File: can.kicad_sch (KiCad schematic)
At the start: 0 parts

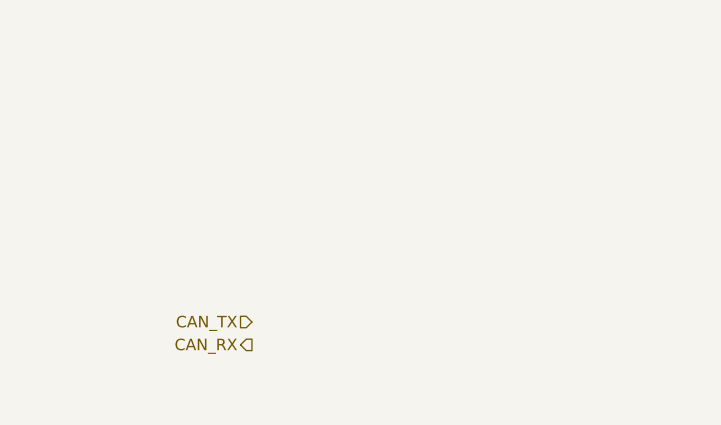
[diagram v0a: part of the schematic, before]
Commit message: Finish schematic
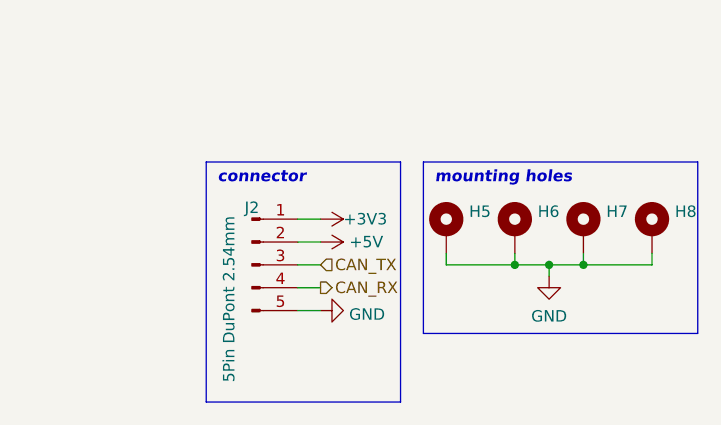
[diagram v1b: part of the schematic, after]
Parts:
- added H5, H6, H7, H8: MountingHole_Pad, MountingHole:MountingHole_3.2mm_M3_Pad_Via, symbol Mechanical:MountingHole_Pad
- added J2: 5Pin DuPont 2.54mm, Connector_PinHeader_2.54mm:PinHeader_1x05_P2.54mm_Vertical, symbol Connector:Conn_01x05_Male
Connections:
- net CAN_RX: now also J2.4 (Pin_4)
- net CAN_TX: now also J2.3 (Pin_3)
- new net +3V3: J2.1 (Pin_1)
- new net +5V: J2.2 (Pin_2)
- new net GND: H5.1, H6.1, H7.1, H8.1, J2.5 (Pin_5)
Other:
- note added: "connector"
- note added: "mounting holes"
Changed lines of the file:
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@@
 (kicad_sch (version 20211123) (generator eeschema)
   (paper "A4")
+  (junction (at 144.78 71.12) (diameter 0) (color 0 0 0 0)
+  )
+  (junction (at 140.97 71.12) (diameter 0) (color 0 0 0 0)
+  )
+  (junction (at 137.16 71.12) (diameter 0) (color 0 0 0 0)
+  )
+  (wire (pts (xy 144.78 71.12) (xy 152.4 71.12))
+    (stroke (width 0) (type default) (color 0 0 0 0))
+  )
+  (wire (pts (xy 113.03 76.2) (xy 115.57 76.2))
+    (stroke (width 0) (type default) (color 0 0 0 0))
+  )
+  (wire (pts (xy 113.03 73.66) (xy 115.57 73.66))
+    (stroke (width 0) (type default) (color 0 0 0 0))
+  )
+  (wire (pts (xy 137.16 69.85) (xy 137.16 71.12))
+    (stroke (width 0) (type default) (color 0 0 0 0))
+  )
+  (polyline (pts (xy 127 59.69) (xy 157.48 59.69))
+    (stroke (width 0) (type default) (color 0 0 0 0))
+  )
+  (polyline (pts (xy 157.48 78.74) (xy 157.48 59.69))
+    (stroke (width 0) (type default) (color 0 0 0 0))
+  )
+  (polyline (pts (xy 102.87 86.36) (xy 124.46 86.36))
+    (stroke (width 0) (type default) (color 0 0 0 0))
+  )
+  (wire (pts (xy 152.4 71.12) (xy 152.4 69.85))
+    (stroke (width 0) (type default) (color 0 0 0 0))
+  )
+  (wire (pts (xy 144.78 69.85) (xy 144.78 71.12))
+    (stroke (width 0) (type default) (color 0 0 0 0))
+  )
+  (wire (pts (xy 113.03 71.12) (xy 115.57 71.12))
+    (stroke (width 0) (type default) (color 0 0 0 0))
+  )
+  (wire (pts (xy 113.03 66.04) (xy 115.57 66.04))
+    (stroke (width 0) (type default) (color 0 0 0 0))
+  )
+  (polyline (pts (xy 102.87 59.69) (xy 124.46 59.69))
+    (stroke (width 0) (type default) (color 0 0 0 0))
+  )
+  (wire (pts (xy 140.97 71.12) (xy 140.97 72.39))
+    (stroke (width 0) (type default) (color 0 0 0 0))
+  )
+  (polyline (pts (xy 124.46 86.36) (xy 124.46 59.69))
+    (stroke (width 0) (type default) (color 0 0 0 0))
+  )
+  (wire (pts (xy 129.54 69.85) (xy 129.54 71.12))
+    (stroke (width 0) (type default) (color 0 0 0 0))
+  )
+  (wire (pts (xy 140.97 71.12) (xy 144.78 71.12))
+    (stroke (width 0) (type default) (color 0 0 0 0))
+  )
+  (wire (pts (xy 113.03 68.58) (xy 115.57 68.58))
+    (stroke (width 0) (type default) (color 0 0 0 0))
+  )
+  (polyline (pts (xy 127 59.69) (xy 127 78.74))
+    (stroke (width 0) (type default) (color 0 0 0 0))
+  )
+  (polyline (pts (xy 127 78.74) (xy 157.48 78.74))
+    (stroke (width 0) (type default) (color 0 0 0 0))
+  )
+  (wire (pts (xy 129.54 71.12) (xy 137.16 71.12))
+    (stroke (width 0) (type default) (color 0 0 0 0))
+  )
+  (polyline (pts (xy 102.87 59.69) (xy 102.87 86.36))
+    (stroke (width 0) (type default) (color 0 0 0 0))
+  )
+  (wire (pts (xy 137.16 71.12) (xy 140.97 71.12))
+    (stroke (width 0) (type default) (color 0 0 0 0))
+  )
+  (text "mounting holes" (at 128.27 62.23 0)
+    (effects (font (size 1.27 1.27) bold italic) (justify left bottom))
+  )
   (text "CAN requierements:\n- galvanic isolation\n- isolated DC/DC converter\n- base is a dedicated PCB due \n  different chip/converter impl. \n  (because semiconductor componts are rare)\n"
     (at 13.97 29.21 0)
     (effects (font (size 1.5 1.5)) (justify left bottom))
   )
-  (hierarchical_label "CAN_TX" (shape input) (at 107.95 77.47 180)
-    (effects (font (size 1.27 1.27)) (justify right))
-  )
-  (hierarchical_label "CAN_RX" (shape output) (at 107.95 80.01 180)
-    (effects (font (size 1.27 1.27)) (justify right))
+  (text "connector" (at 104.14 62.23 0)
+    (effects (font (size 1.27 1.27) bold italic) (justify left bottom))
+  )
+  (hierarchical_label "CAN_TX" (shape input) (at 115.57 71.12 0)
+    (effects (font (size 1.27 1.27)) (justify left))
+  )
+  (hierarchical_label "CAN_RX" (shape output) (at 115.57 73.66 0)
+    (effects (font (size 1.27 1.27)) (justify left))
+  )
+  (symbol (lib_id "Mechanical:MountingHole_Pad") (at 137.16 67.31 0) (unit 1)
+    (in_bom yes) (on_board yes) (fields_autoplaced)
+    (property "Reference" "H6" (id 0) (at 139.7 65.2053 0)
+      (effects (font (size 1.27 1.27)) (justify left))
+    )
+    (property "Value" "MountingHole_Pad" (id 1) (at 139.7 67.7422 0)
+      (effects (font (size 1.27 1.27)) (justify left) hide)
+    )
+    (property "Footprint" "MountingHole:MountingHole_3.2mm_M3_Pad_Via" (id 2) (at 137.16 67.31 0)
+      (effects (font (size 1.27 1.27)) hide)
+    )
+    (property "Datasheet" "~" (id 3) (at 137.16 67.31 0)
+      (effects (font (size 1.27 1.27)) hide)
+    )
+    (pin "1")
+  )
+  (symbol (lib_id "power:+5V") (at 115.57 68.58 270) (unit 1)
+    (in_bom yes) (on_board yes)
+    (property "Reference" "#PWR019" (id 0) (at 111.76 68.58 0)
+      (effects (font (size 1.27 1.27)) hide)
+    )
+    (property "Value" "+5V" (id 1) (at 120.65 68.58 90))
+    (property "Footprint" "" (id 2) (at 115.57 68.58 0)
+      (effects (font (size 1.27 1.27)) hide)
+    )
+    (property "Datasheet" "" (id 3) (at 115.57 68.58 0)
+      (effects (font (size 1.27 1.27)) hide)
+    )
+    (pin "1")
+  )
+  (symbol (lib_id "power:GND") (at 115.57 76.2 90) (unit 1)
+    (in_bom yes) (on_board yes) (fields_autoplaced)
+    (property "Reference" "#PWR021" (id 0) (at 121.92 76.2 0)
+      (effects (font (size 1.27 1.27)) hide)
+    )
+    (property "Value" "GND" (id 1) (at 118.745 76.6338 90)
+      (effects (font (size 1.27 1.27)) (justify right))
+    )
+    (property "Footprint" "" (id 2) (at 115.57 76.2 0)
+      (effects (font (size 1.27 1.27)) hide)
+    )
+    (property "Datasheet" "" (id 3) (at 115.57 76.2 0)
+      (effects (font (size 1.27 1.27)) hide)
+    )
+    (pin "1")
+  )
+  (symbol (lib_id "power:GND") (at 140.97 72.39 0) (unit 1)
+    (in_bom yes) (on_board yes) (fields_autoplaced)
+    (property "Reference" "#PWR020" (id 0) (at 140.97 78.74 0)
+      (effects (font (size 1.27 1.27)) hide)
+    )
+    (property "Value" "GND" (id 1) (at 140.97 76.8334 0))
+    (property "Footprint" "" (id 2) (at 140.97 72.39 0)
+      (effects (font (size 1.27 1.27)) hide)
+    )
+    (property "Datasheet" "" (id 3) (at 140.97 72.39 0)
+      (effects (font (size 1.27 1.27)) hide)
+    )
+    (pin "1")
+  )
+  (symbol (lib_id "Mechanical:MountingHole_Pad") (at 152.4 67.31 0) (unit 1)
+    (in_bom yes) (on_board yes) (fields_autoplaced)
+    (property "Reference" "H8" (id 0) (at 154.94 65.2053 0)
+      (effects (font (size 1.27 1.27)) (justify left))
+    )
+    (property "Value" "MountingHole_Pad" (id 1) (at 154.94 67.7422 0)
+      (effects (font (size 1.27 1.27)) (justify left) hide)
+    )
+    (property "Footprint" "MountingHole:MountingHole_3.2mm_M3_Pad_Via" (id 2) (at 152.4 67.31 0)
+      (effects (font (size 1.27 1.27)) hide)
+    )
+    (property "Datasheet" "~" (id 3) (at 152.4 67.31 0)
+      (effects (font (size 1.27 1.27)) hide)
+    )
+    (pin "1")
+  )
+  (symbol (lib_id "Mechanical:MountingHole_Pad") (at 144.78 67.31 0) (unit 1)
+    (in_bom yes) (on_board yes) (fields_autoplaced)
+    (property "Reference" "H7" (id 0) (at 147.32 65.2053 0)
+      (effects (font (size 1.27 1.27)) (justify left))
+    )
+    (property "Value" "MountingHole_Pad" (id 1) (at 147.32 67.7422 0)
+      (effects (font (size 1.27 1.27)) (justify left) hide)
+    )
+    (property "Footprint" "MountingHole:MountingHole_3.2mm_M3_Pad_Via" (id 2) (at 144.78 67.31 0)
+      (effects (font (size 1.27 1.27)) hide)
+    )
+    (property "Datasheet" "~" (id 3) (at 144.78 67.31 0)
+      (effects (font (size 1.27 1.27)) hide)
+    )
+    (pin "1")
+  )
+  (symbol (lib_id "power:+3V3") (at 115.57 66.04 270) (unit 1)
+    (in_bom yes) (on_board yes)
+    (property "Reference" "#PWR018" (id 0) (at 111.76 66.04 0)
+      (effects (font (size 1.27 1.27)) hide)
+    )
+    (property "Value" "+3V3" (id 1) (at 118.11 66.04 90)
+      (effects (font (size 1.27 1.27)) (justify left))
+    )
+    (property "Footprint" "" (id 2) (at 115.57 66.04 0)
+      (effects (font (size 1.27 1.27)) hide)
+    )
+    (property "Datasheet" "" (id 3) (at 115.57 66.04 0)
+      (effects (font (size 1.27 1.27)) hide)
+    )
+    (pin "1")
+  )
+  (symbol (lib_id "Connector:Conn_01x05_Male") (at 107.95 71.12 0) (unit 1)
+    (in_bom yes) (on_board yes)
+    (property "Reference" "J2" (id 0) (at 107.95 64.77 0))
+    (property "Value" "5Pin DuPont 2.54mm" (id 1) (at 105.41 74.93 90))
+    (property "Footprint" "Connector_PinHeader_2.54mm:PinHeader_1x05_P2.54mm_Vertical" (id 2) (at 107.95 71.12 0)
+      (effects (font (size 1.27 1.27)) hide)
+    )
+    (property "Datasheet" "~" (id 3) (at 107.95 71.12 0)
+      (effects (font (size 1.27 1.27)) hide)
+    )
+    (pin "1")
+    (pin "2")
+    (pin "3")
+    (pin "4")
+    (pin "5")
+  )
+  (symbol (lib_id "Mechanical:MountingHole_Pad") (at 129.54 67.31 0) (unit 1)
+    (in_bom yes) (on_board yes) (fields_autoplaced)
+    (property "Reference" "H5" (id 0) (at 132.08 65.2053 0)
+      (effects (font (size 1.27 1.27)) (justify left))
+    )
+    (property "Value" "MountingHole_Pad" (id 1) (at 132.08 67.7422 0)
+      (effects (font (size 1.27 1.27)) (justify left) hide)
+    )
+    (property "Footprint" "MountingHole:MountingHole_3.2mm_M3_Pad_Via" (id 2) (at 129.54 67.31 0)
+      (effects (font (size 1.27 1.27)) hide)
+    )
+    (property "Datasheet" "~" (id 3) (at 129.54 67.31 0)
+      (effects (font (size 1.27 1.27)) hide)
+    )
+    (pin "1")
   )
 )

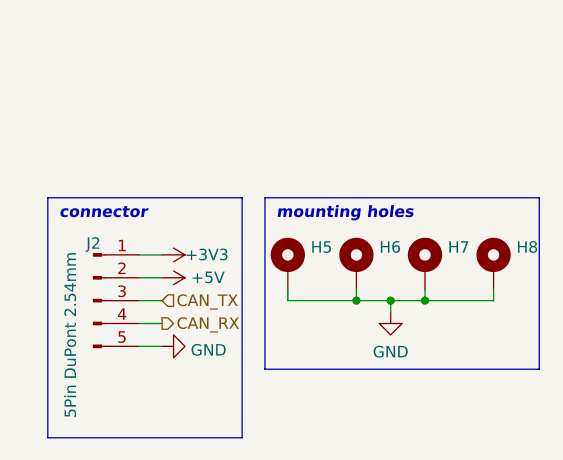
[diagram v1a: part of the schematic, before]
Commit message: Add many changes to schematic and WIP PCB
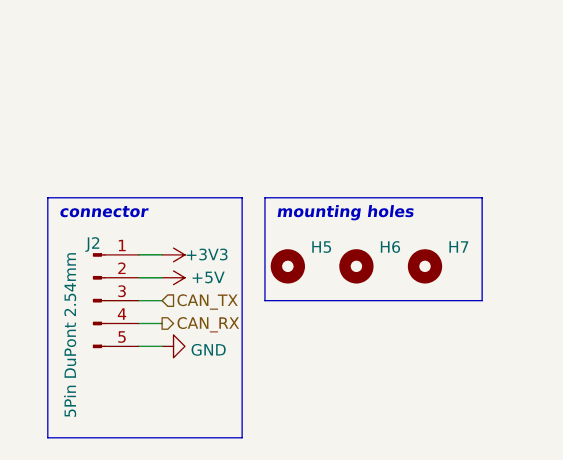
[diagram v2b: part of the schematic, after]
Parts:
- removed H8: MountingHole_Pad, MountingHole:MountingHole_3.2mm_M3_Pad_Via, symbol Mechanical:MountingHole_Pad
- H5, H6, H7: footprint MountingHole:MountingHole_3.2mm_M3_Pad_Via -> MountingHole:MountingHole_3.2mm_M3_ISO14580; symbol Mechanical:MountingHole_Pad -> Mechanical:MountingHole
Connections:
- net GND: no longer H5.1, H6.1, H7.1
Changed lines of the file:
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@@
 (kicad_sch (version 20211123) (generator eeschema)
   (paper "A4")
-  (junction (at 144.78 71.12) (diameter 0) (color 0 0 0 0)
-  )
-  (junction (at 140.97 71.12) (diameter 0) (color 0 0 0 0)
-  )
-  (junction (at 137.16 71.12) (diameter 0) (color 0 0 0 0)
-  )
-  (wire (pts (xy 144.78 71.12) (xy 152.4 71.12))
-    (stroke (width 0) (type default) (color 0 0 0 0))
-  )
   (wire (pts (xy 113.03 76.2) (xy 115.57 76.2))
     (stroke (width 0) (type default) (color 0 0 0 0))
@@
     (stroke (width 0) (type default) (color 0 0 0 0))
   )
-  (wire (pts (xy 137.16 69.85) (xy 137.16 71.12))
+  (polyline (pts (xy 127 59.69) (xy 151.13 59.69))
     (stroke (width 0) (type default) (color 0 0 0 0))
   )
-  (polyline (pts (xy 127 59.69) (xy 157.48 59.69))
-    (stroke (width 0) (type default) (color 0 0 0 0))
-  )
-  (polyline (pts (xy 157.48 78.74) (xy 157.48 59.69))
+  (polyline (pts (xy 151.13 71.12) (xy 151.13 59.69))
     (stroke (width 0) (type default) (color 0 0 0 0))
   )
   (polyline (pts (xy 102.87 86.36) (xy 124.46 86.36))
-    (stroke (width 0) (type default) (color 0 0 0 0))
-  )
-  (wire (pts (xy 152.4 71.12) (xy 152.4 69.85))
-    (stroke (width 0) (type default) (color 0 0 0 0))
-  )
-  (wire (pts (xy 144.78 69.85) (xy 144.78 71.12))
     (stroke (width 0) (type default) (color 0 0 0 0))
   )
@@
     (stroke (width 0) (type default) (color 0 0 0 0))
   )
-  (wire (pts (xy 140.97 71.12) (xy 140.97 72.39))
-    (stroke (width 0) (type default) (color 0 0 0 0))
-  )
   (polyline (pts (xy 124.46 86.36) (xy 124.46 59.69))
-    (stroke (width 0) (type default) (color 0 0 0 0))
-  )
-  (wire (pts (xy 129.54 69.85) (xy 129.54 71.12))
-    (stroke (width 0) (type default) (color 0 0 0 0))
-  )
-  (wire (pts (xy 140.97 71.12) (xy 144.78 71.12))
     (stroke (width 0) (type default) (color 0 0 0 0))
   )
@@
     (stroke (width 0) (type default) (color 0 0 0 0))
   )
-  (polyline (pts (xy 127 59.69) (xy 127 78.74))
+  (polyline (pts (xy 127 59.69) (xy 127 71.12))
     (stroke (width 0) (type default) (color 0 0 0 0))
   )
-  (polyline (pts (xy 127 78.74) (xy 157.48 78.74))
-    (stroke (width 0) (type default) (color 0 0 0 0))
-  )
-  (wire (pts (xy 129.54 71.12) (xy 137.16 71.12))
+  (polyline (pts (xy 127 71.12) (xy 151.13 71.12))
     (stroke (width 0) (type default) (color 0 0 0 0))
   )
   (polyline (pts (xy 102.87 59.69) (xy 102.87 86.36))
-    (stroke (width 0) (type default) (color 0 0 0 0))
-  )
-  (wire (pts (xy 137.16 71.12) (xy 140.97 71.12))
     (stroke (width 0) (type default) (color 0 0 0 0))
   )
@@
     (effects (font (size 1.27 1.27)) (justify left))
   )
-  (symbol (lib_id "Mechanical:MountingHole_Pad") (at 137.16 67.31 0) (unit 1)
+  (symbol (lib_id "Mechanical:MountingHole") (at 137.16 67.31 0) (unit 1)
     (in_bom yes) (on_board yes) (fields_autoplaced)
     (property "Reference" "H6" (id 0) (at 139.7 65.2053 0)
@@
       (effects (font (size 1.27 1.27)) (justify left) hide)
     )
-    (property "Footprint" "MountingHole:MountingHole_3.2mm_M3_Pad_Via" (id 2) (at 137.16 67.31 0)
+    (property "Footprint" "MountingHole:MountingHole_3.2mm_M3_ISO14580" (id 2) (at 137.16 67.31 0)
       (effects (font (size 1.27 1.27)) hide)
     )
@@
       (effects (font (size 1.27 1.27)) hide)
     )
-    (pin "1")
   )
   (symbol (lib_id "power:+5V") (at 115.57 68.58 270) (unit 1)
     (in_bom yes) (on_board yes)
-    (property "Reference" "#PWR019" (id 0) (at 111.76 68.58 0)
+    (property "Reference" "#PWR0118" (id 0) (at 111.76 68.58 0)
       (effects (font (size 1.27 1.27)) hide)
     )
@@
   (symbol (lib_id "power:GND") (at 115.57 76.2 90) (unit 1)
     (in_bom yes) (on_board yes) (fields_autoplaced)
-    (property "Reference" "#PWR021" (id 0) (at 121.92 76.2 0)
+    (property "Reference" "#PWR0120" (id 0) (at 121.92 76.2 0)
       (effects (font (size 1.27 1.27)) hide)
     )
@@
     (pin "1")
   )
-  (symbol (lib_id "power:GND") (at 140.97 72.39 0) (unit 1)
-    (in_bom yes) (on_board yes) (fields_autoplaced)
-    (property "Reference" "#PWR020" (id 0) (at 140.97 78.74 0)
-      (effects (font (size 1.27 1.27)) hide)
-    )
-    (property "Value" "GND" (id 1) (at 140.97 76.8334 0))
-    (property "Footprint" "" (id 2) (at 140.97 72.39 0)
-      (effects (font (size 1.27 1.27)) hide)
-    )
-    (property "Datasheet" "" (id 3) (at 140.97 72.39 0)
-      (effects (font (size 1.27 1.27)) hide)
-    )
-    (pin "1")
-  )
-  (symbol (lib_id "Mechanical:MountingHole_Pad") (at 152.4 67.31 0) (unit 1)
-    (in_bom yes) (on_board yes) (fields_autoplaced)
-    (property "Reference" "H8" (id 0) (at 154.94 65.2053 0)
-      (effects (font (size 1.27 1.27)) (justify left))
-    )
-    (property "Value" "MountingHole_Pad" (id 1) (at 154.94 67.7422 0)
-      (effects (font (size 1.27 1.27)) (justify left) hide)
-    )
-    (property "Footprint" "MountingHole:MountingHole_3.2mm_M3_Pad_Via" (id 2) (at 152.4 67.31 0)
-      (effects (font (size 1.27 1.27)) hide)
-    )
-    (property "Datasheet" "~" (id 3) (at 152.4 67.31 0)
-      (effects (font (size 1.27 1.27)) hide)
-    )
-    (pin "1")
-  )
-  (symbol (lib_id "Mechanical:MountingHole_Pad") (at 144.78 67.31 0) (unit 1)
+  (symbol (lib_id "Mechanical:MountingHole") (at 144.78 67.31 0) (unit 1)
     (in_bom yes) (on_board yes) (fields_autoplaced)
     (property "Reference" "H7" (id 0) (at 147.32 65.2053 0)
@@
       (effects (font (size 1.27 1.27)) (justify left) hide)
     )
-    (property "Footprint" "MountingHole:MountingHole_3.2mm_M3_Pad_Via" (id 2) (at 144.78 67.31 0)
+    (property "Footprint" "MountingHole:MountingHole_3.2mm_M3_ISO14580" (id 2) (at 144.78 67.31 0)
       (effects (font (size 1.27 1.27)) hide)
     )
@@
       (effects (font (size 1.27 1.27)) hide)
     )
-    (pin "1")
   )
   (symbol (lib_id "power:+3V3") (at 115.57 66.04 270) (unit 1)
     (in_bom yes) (on_board yes)
-    (property "Reference" "#PWR018" (id 0) (at 111.76 66.04 0)
+    (property "Reference" "#PWR0119" (id 0) (at 111.76 66.04 0)
       (effects (font (size 1.27 1.27)) hide)
     )
@@
     (pin "5")
   )
-  (symbol (lib_id "Mechanical:MountingHole_Pad") (at 129.54 67.31 0) (unit 1)
+  (symbol (lib_id "Mechanical:MountingHole") (at 129.54 67.31 0) (unit 1)
     (in_bom yes) (on_board yes) (fields_autoplaced)
     (property "Reference" "H5" (id 0) (at 132.08 65.2053 0)
@@
       (effects (font (size 1.27 1.27)) (justify left) hide)
     )
-    (property "Footprint" "MountingHole:MountingHole_3.2mm_M3_Pad_Via" (id 2) (at 129.54 67.31 0)
+    (property "Footprint" "MountingHole:MountingHole_3.2mm_M3_ISO14580" (id 2) (at 129.54 67.31 0)
       (effects (font (size 1.27 1.27)) hide)
     )
@@
       (effects (font (size 1.27 1.27)) hide)
     )
-    (pin "1")
   )
 )
